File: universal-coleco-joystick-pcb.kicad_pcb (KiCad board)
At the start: 2 copper layers, 108 x 62.3 mm, 49 parts, among them J1 Sanwa Joystick, J2 DE9_Receptacle, J3 Conn_01x09_Socket, SW1 Arm, SW10 2, SW11 #, SW12 9, SW13 6, SW14 3, SW2 Fire, SW3 *, SW4 7, SW5 1, SW6 4, SW7 0, SW8 8, SW9 5

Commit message: Credit
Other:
- board text added: "1"
- board text added: "2"
- board text added: "3"
- board text added: "4"
- board text added: "5"
- board text added: "6"
- board text added: "7"
- board text added: "8"
- board text added: "9"
- board text added: "CV DIY Joystick (Sanwa Edition) v1 leadedsolder.com 2024"
- board text added: "Female DE9 (optional)"
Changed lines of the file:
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@@
 		(tags "Diode DO-41_SOD81 series Axial Horizontal pin pitch 10.16mm  length 5.2mm diameter 2.7mm")
 		(property "Reference" "D24"
-			(at 5.08 0 360)
+			(at 5.08 0 0)
 			(layer "F.SilkS")
 			(effects
@@
 		)
 		(property "Value" "D_45deg"
-			(at 5.08 2.47 360)
+			(at 5.08 2.47 0)
 			(layer "F.Fab")
 			(effects
@@
 		)
 		(fp_text user "${REFERENCE}"
-			(at 5.47 0 360)
+			(at 5.47 0 0)
 			(layer "F.Fab")
 			(effects
@@
 		)
 		(fp_text user "K"
-			(at 0 -2.1 360)
+			(at 0 -2.1 0)
 			(layer "F.Fab")
 			(effects
@@
 		(tags "9-pin D-Sub connector horizontal angled 90deg THT female pitch 2.77x2.84mm pin-PCB-offset 7.699999999999999mm mounting-holes-distance 25mm mounting-hole-offset 25mm")
 		(property "Reference" "J2"
-			(at -5.54 -2.8 360)
+			(at -5.54 -2.8 0)
 			(layer "F.SilkS")
 			(effects
@@
 		)
 		(property "Value" "DE9_Receptacle"
-			(at -5.54 18.61 360)
+			(at -5.54 18.61 0)
 			(layer "F.Fab")
 			(effects
@@
 		)
 		(fp_text user "${REFERENCE}"
-			(at -5.54 14.025 360)
+			(at -5.54 14.025 0)
 			(layer "F.Fab")
 			(effects
@@
 		)
 		(fp_text user "${REFERENCE}"
-			(at 0 10.16 360)
+			(at 0 10.16 0)
 			(layer "F.Fab")
 			(effects
@@
 		(layer "Edge.Cuts")
 	)
+	(gr_text "3"
+		(at 136.525 74.93 0)
+		(layer "B.SilkS")
+		(effects
+			(font
+				(size 1 1)
+				(thickness 0.1)
+			)
+			(justify left bottom mirror)
+		)
+	)
+	(gr_text "4"
+		(at 139.065 74.93 0)
+		(layer "B.SilkS")
+		(effects
+			(font
+				(size 1 1)
+				(thickness 0.1)
+			)
+			(justify left bottom mirror)
+		)
+	)
+	(gr_text "8"
+		(at 137.795 68.58 0)
+		(layer "B.SilkS")
+		(effects
+			(font
+				(size 1 1)
+				(thickness 0.1)
+			)
+			(justify left bottom mirror)
+		)
+	)
+	(gr_text "9"
+		(at 140.335 68.58 0)
+		(layer "B.SilkS")
+		(effects
+			(font
+				(size 1 1)
+				(thickness 0.1)
+			)
+			(justify left bottom mirror)
+		)
+	)
+	(gr_text "2"
+		(at 133.35 74.93 0)
+		(layer "B.SilkS")
+		(effects
+			(font
+				(size 1 1)
+				(thickness 0.1)
+			)
+			(justify left bottom mirror)
+		)
+	)
+	(gr_text "1"
+		(at 130.81 74.93 0)
+		(layer "B.SilkS")
+		(effects
+			(font
+				(size 1 1)
+				(thickness 0.1)
+			)
+			(justify left bottom mirror)
+		)
+	)
+	(gr_text "7"
+		(at 134.62 68.58 0)
+		(layer "B.SilkS")
+		(effects
+			(font
+				(size 1 1)
+				(thickness 0.1)
+			)
+			(justify left bottom mirror)
+		)
+	)
+	(gr_text "5"
+		(at 142.875 74.93 0)
+		(layer "B.SilkS")
+		(effects
+			(font
+				(size 1 1)
+				(thickness 0.1)
+			)
+			(justify left bottom mirror)
+		)
+	)
+	(gr_text "6"
+		(at 132.08 68.58 0)
+		(layer "B.SilkS")
+		(effects
+			(font
+				(size 1 1)
+				(thickness 0.1)
+			)
+			(justify left bottom mirror)
+		)
+	)
+	(gr_text "CV DIY Joystick (Sanwa Edition) v1 leadedsolder.com 2024"
+		(at 90.805 121.285 0)
+		(layer "F.SilkS")
+		(effects
+			(font
+				(size 1 1)
+				(thickness 0.1)
+			)
+			(justify left bottom)
+		)
+	)
 	(gr_text "Down"
 		(at 88.9 72.39 0)
@@
 		(layer "F.SilkS")
 		(effects
+			(font
+				(size 1 1)
+				(thickness 0.1)
+			)
+			(justify left bottom)
+		)
+	)
+	(gr_text "Female DE9 (optional)"
+		(at 127.635 66.04 0)
+		(layer "F.SilkS")
+		(effects

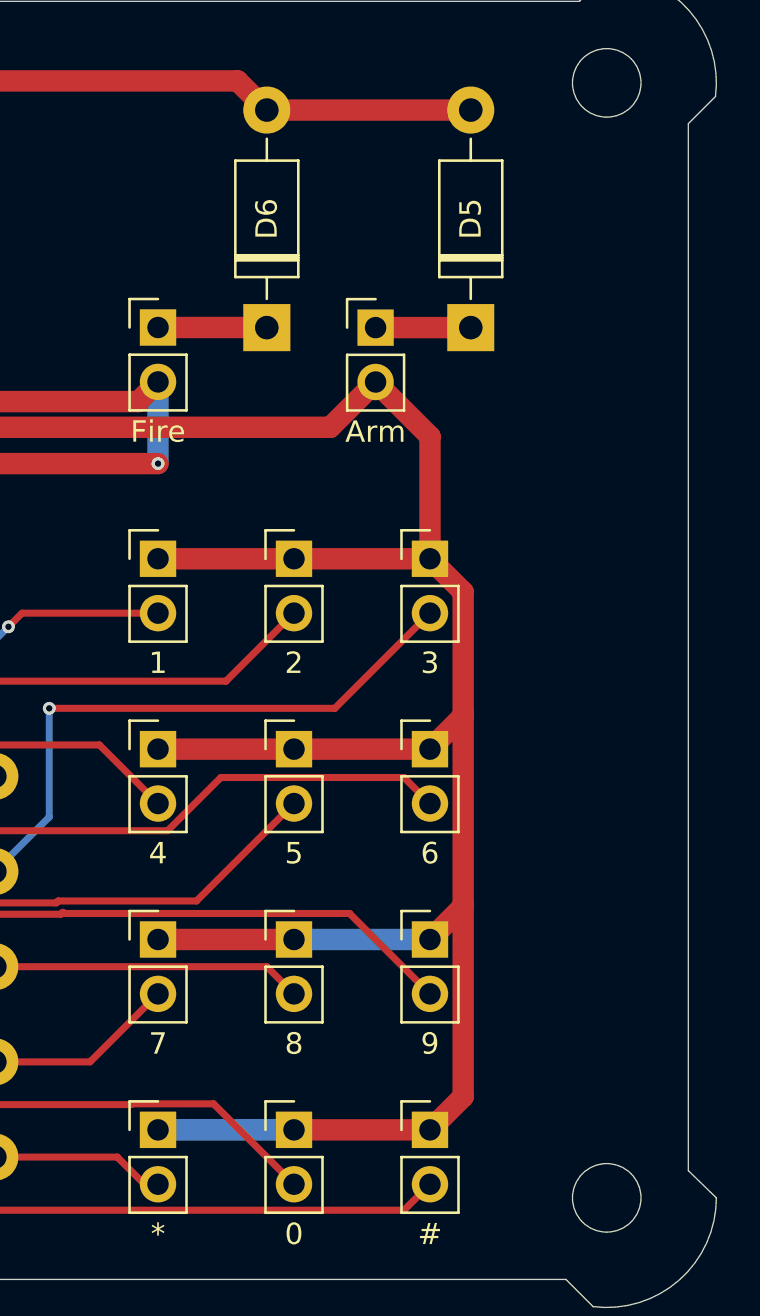
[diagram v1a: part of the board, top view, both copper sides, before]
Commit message: Linear KP header
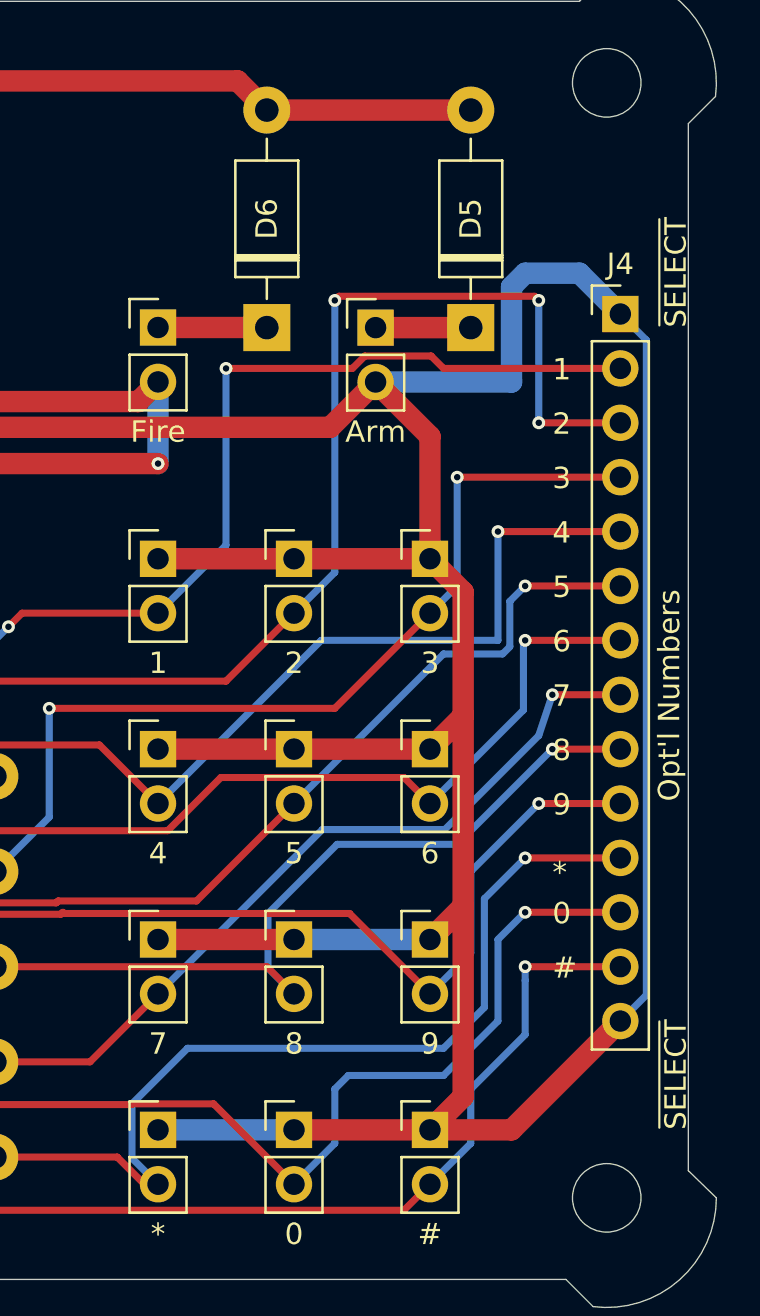
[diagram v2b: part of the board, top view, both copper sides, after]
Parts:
- added J4: Opt'l Numbers, Connector_PinHeader_2.54mm:PinHeader_1x14_P2.54mm_Vertical, F.Cu at (185.4, 76.8)
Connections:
- net Net-(D10-A) renamed /KP_7
- net Net-(D11-A) renamed /KP_1
- net Net-(D17-A) renamed /KP_8
- net Net-(D27-A) renamed /KP_3
- net Net-(D7-A) renamed /KP_STAR
- D12 pad 2: unconnected-(D12-A-Pad2) -> /KP_4
- D13 pad 2: unconnected-(D12-A-Pad2) -> /KP_4
- D14 pad 2: unconnected-(D12-A-Pad2) -> /KP_4
- D15 pad 2: unconnected-(D15-A-Pad2) -> /KP_0
- D16 pad 2: unconnected-(D15-A-Pad2) -> /KP_0
- D20 pad 2: unconnected-(D20-A-Pad2) -> /KP_5
- D21 pad 2: unconnected-(D20-A-Pad2) -> /KP_5
- D22 pad 2: unconnected-(D22-A-Pad2) -> /KP_2
- D23 pad 2: unconnected-(D23-A-Pad2) -> /KP_OCTOTHORPE
- D24 pad 2: unconnected-(D23-A-Pad2) -> /KP_OCTOTHORPE
- D25 pad 2: unconnected-(D25-A-Pad2) -> /KP_9
- D26 pad 2: unconnected-(D26-A-Pad2) -> /KP_6
- SW10 pad 2: unconnected-(D22-A-Pad2) -> /KP_2
- SW11 pad 2: unconnected-(D23-A-Pad2) -> /KP_OCTOTHORPE
- SW12 pad 2: unconnected-(D25-A-Pad2) -> /KP_9
- SW13 pad 2: unconnected-(D26-A-Pad2) -> /KP_6
- SW6 pad 2: unconnected-(D12-A-Pad2) -> /KP_4
- SW7 pad 2: unconnected-(D15-A-Pad2) -> /KP_0
- SW9 pad 2: unconnected-(D20-A-Pad2) -> /KP_5
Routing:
- net /KP_4: track 0.00 -> 82.2 mm, vias 0 -> 1
- net /KP_0: track 0.00 -> 81.8 mm, vias 0 -> 1
- net /KP_OCTOTHORPE: track 0.00 -> 79.5 mm, vias 0 -> 1
- net /KP_6: track 0.00 -> 76.8 mm, vias 0 -> 1
- net /KP_5: track 0.00 -> 69.7 mm, vias 0 -> 2
- net /KP_9: track 0.00 -> 65.0 mm, vias 0 -> 1
- net /KP_2: track 0.00 -> 63.2 mm, vias 0 -> 3
- net unconnected-(D23-A-Pad2): track 63.1 -> 0.00 mm
- net unconnected-(D26-A-Pad2): track 62.9 -> 0.00 mm
- net /~{Select}: track 141.6 -> 203.6 mm
- net unconnected-(D15-A-Pad2): track 57.6 -> 0.00 mm
- net unconnected-(D12-A-Pad2): track 52.4 -> 0.00 mm
- net unconnected-(D25-A-Pad2): track 50.2 -> 0.00 mm
- net unconnected-(D20-A-Pad2): track 49.0 -> 0.00 mm, vias 1 -> 0
- net /KP_STAR: track 36.0 -> 70.8 mm, vias 0 -> 1
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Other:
- board text added: "#"
- board text added: "*"
- board text added: "0"
- board text added: "~{SELECT}"

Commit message: Release v1 to JLC
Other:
- board text added: "2024-v1"
- board text added: "CV DIY Control leadedsolder.com"
- board text removed: "CV DIY Joystick (Sanwa Edition) v1 leadedsolder.com 2024"
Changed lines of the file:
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@@
 			(outputformat 1)
 			(mirror no)
-			(drillshape 1)
+			(drillshape 0)
 			(scaleselection 1)
-			(outputdirectory "")
+			(outputdirectory "cv-diy-joystick-proto1")
 		)
 	)
@@
 		)
 	)
+	(gr_rect
+		(start 94.615 91.44)
+		(end 100.33 120.015)
+		(stroke
+			(width 0.1)
+			(type solid)
+		)
+		(fill solid)
+		(layer "F.SilkS")
+	)
 	(gr_arc
 		(start 86.995 123.229533)
@@
 		)
 	)
-	(gr_text "CV DIY Joystick (Sanwa Edition) v1 leadedsolder.com 2024"
-		(at 90.805 121.285 0)
+	(gr_text "CV DIY Control\nleadedsolder.com"
+		(at 94 80.6 90)
 		(layer "F.SilkS")
 		(effects
 			(font
-				(size 1 1)
-				(thickness 0.1)
+				(size 3 3)
+				(thickness 0.5)
+				(bold yes)
+				(italic yes)
 			)
-			(justify left bottom)
+			(justify right bottom)
 		)
 	)
@@
 		(effects
 			(font
+				(size 1 1)
+				(thickness 0.1)
+			)
+			(justify left bottom)
+		)
+	)
+	(gr_text "2024-v1"
+		(at 96.52 90.805 90)
+		(layer "F.SilkS")
+		(effects
+			(font

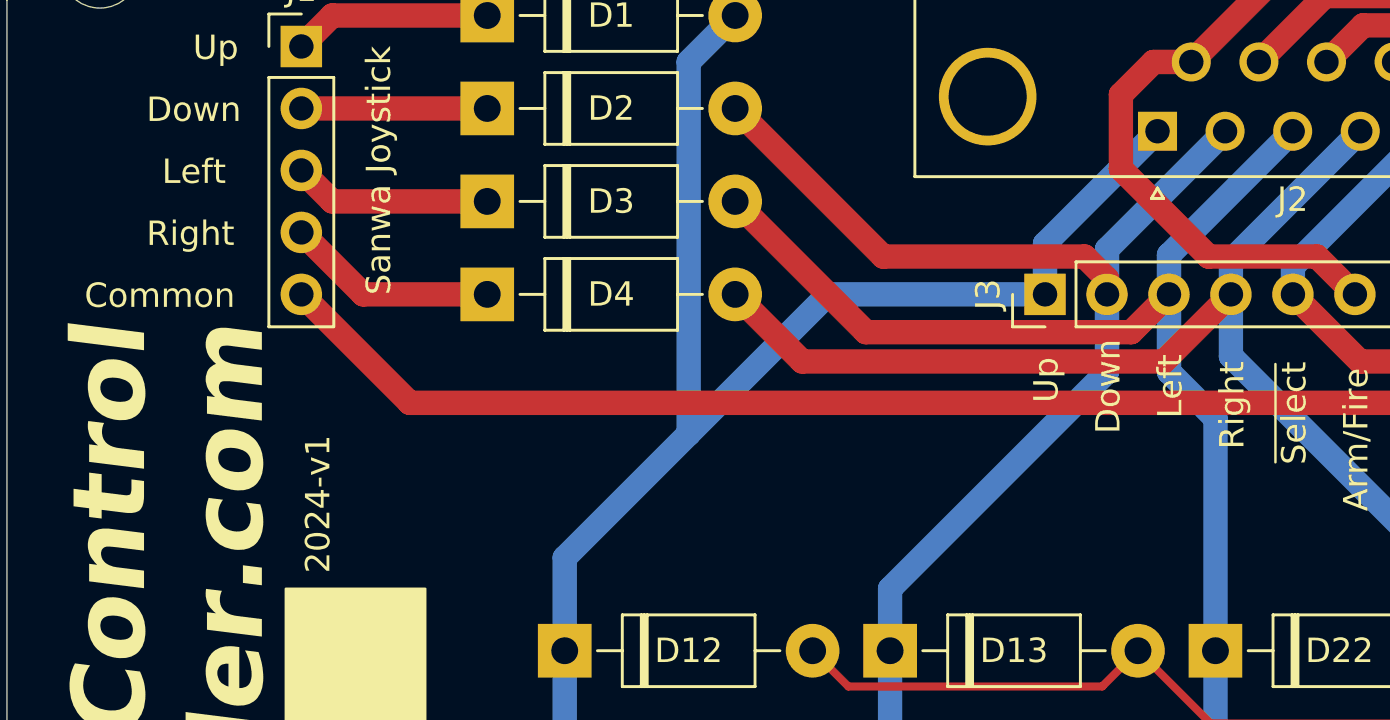
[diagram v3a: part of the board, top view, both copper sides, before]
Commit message: UDRL not UDLR joystick error
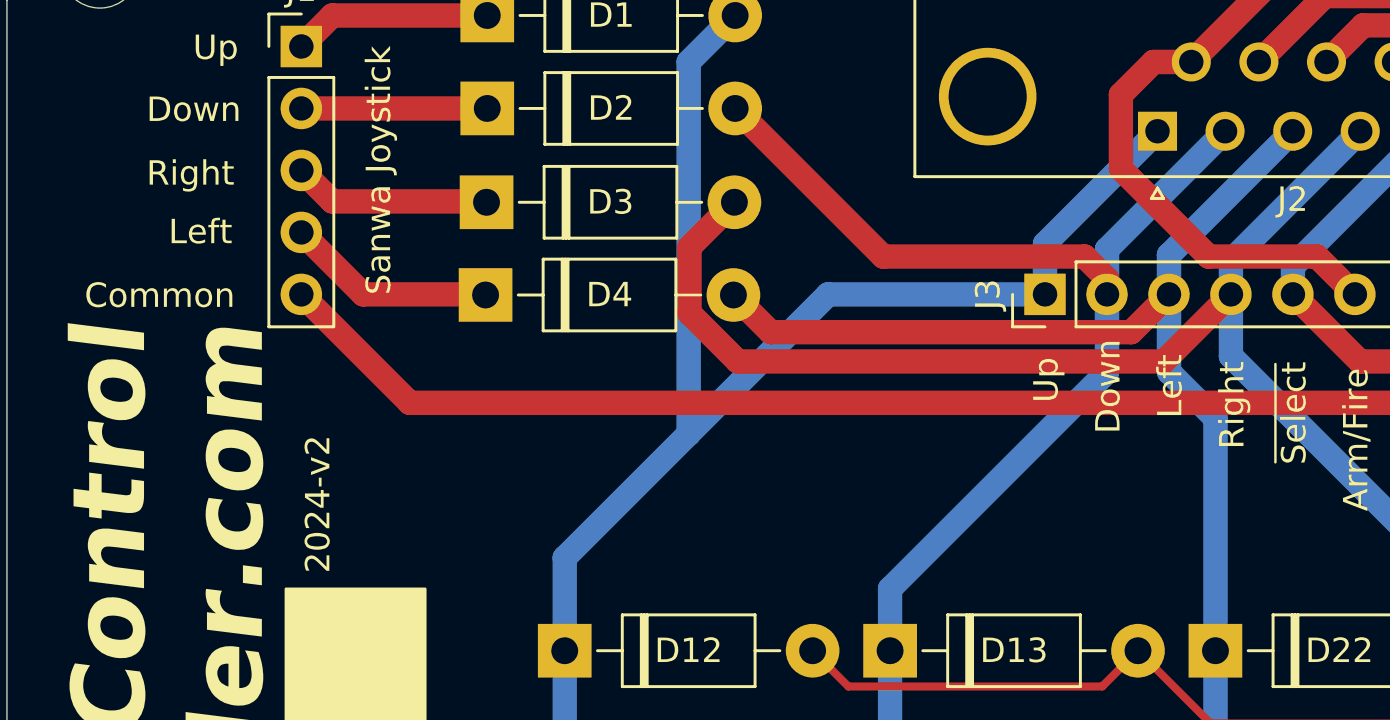
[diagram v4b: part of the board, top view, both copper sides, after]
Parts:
- moved D4 0.07 mm to (102.8, 79.4)
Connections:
- D3 pad 2: /Left -> /Right
- D4 pad 2: /Right -> /Left
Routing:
- net /Right: track 73.6 -> 80.4 mm
- net /Left: track 67.0 -> 65.5 mm
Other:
- board text added: "2024-v2"
- board text removed: "2024-v1"
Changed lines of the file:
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@@
 	(footprint "Diode_THT:D_DO-41_SOD81_P10.16mm_Horizontal"
 		(layer "F.Cu")
-		(at 102.87 79.375)
+		(at 102.8 79.4)
 		(descr "Diode, DO-41_SOD81 series, Axial, Horizontal, pin pitch=10.16mm, , length*diameter=5.2*2.7mm^2, , http://www.diodes.com/_files/packages/DO-41%20(Plastic).pdf")
 		(tags "Diode DO-41_SOD81 series Axial Horizontal pin pitch 10.16mm  length 5.2mm diameter 2.7mm")
@@
 			(layers "*.Cu" "*.Mask")
 			(remove_unused_layers no)
-			(net 8 "/Right")
+			(net 5 "/Left")
 			(pinfunction "A")
 			(pintype "passive")
@@
 	(footprint "Diode_THT:D_DO-41_SOD81_P10.16mm_Horizontal"
 		(layer "F.Cu")
-		(at 102.87 75.565)
+		(at 102.84 75.6)
 		(descr "Diode, DO-41_SOD81 series, Axial, Horizontal, pin pitch=10.16mm, , length*diameter=5.2*2.7mm^2, , http://www.diodes.com/_files/packages/DO-41%20(Plastic).pdf")
 		(tags "Diode DO-41_SOD81 series Axial Horizontal pin pitch 10.16mm  length 5.2mm diameter 2.7mm")
@@
 			(layers "*.Cu" "*.Mask")
 			(remove_unused_layers no)
-			(net 5 "/Left")
+			(net 8 "/Right")
 			(pinfunction "A")
 			(pintype "passive")
@@
 	(gr_text "Common"
 		(at 86.36 80.01 0)
-		(layer "F.SilkS")
+		(layer "F.SilkS" knockout)
 		(effects
 			(font
@@
 	)
 	(gr_text "Right"
-		(at 88.9 77.47 0)
+		(at 88.9 75 0)
 		(layer "F.SilkS")
 		(effects
@@
 	)
 	(gr_text "Left"
-		(at 89.535 74.93 0)
+		(at 89.8 77.4 0)
 		(layer "F.SilkS")
 		(effects
@@
 		)
 	)
-	(gr_text "2024-v1"
+	(gr_text "2024-v2"
 		(at 96.52 90.805 90)
 		(layer "F.SilkS")
@@
 	(segment
 		(start 129.26 80.925)
-		(end 118.39 80.925)
+		(end 114.485 80.925)
 		(width 1)
 		(layer "F.Cu")
@@
 	)
 	(segment
-		(start 130.81 79.375)
-		(end 129.26 80.925)
+		(start 114.485 80.925)
+		(end 112.96 79.4)
 		(width 1)
 		(layer "F.Cu")
@@
 	)
 	(segment
-		(start 118.39 80.925)
-		(end 113.03 75.565)
+		(start 130.81 79.375)
+		(end 129.26 80.925)
 		(width 1)
 		(layer "F.Cu")
@@
 	)
 	(segment
-		(start 115.78 82.125)
+		(start 111.16 80.145585)
+		(end 111.16 77.44)
+		(width 1)
+		(layer "F.Cu")
+		(net 8)
+	)
+	(segment
+		(start 130.6 82.125)
+		(end 113.139415 82.125)
+		(width 1)
+		(layer "F.Cu")
+		(net 8)
+	)
+	(segment
+		(start 133.35 79.375)
 		(end 130.6 82.125)
 		(width 1)
@@
 	)
 	(segment
-		(start 113.03 79.375)
-		(end 115.78 82.125)
+		(start 111.16 77.44)
+		(end 113 75.6)
 		(width 1)
 		(layer "F.Cu")
@@
 	)
 	(segment
-		(start 130.6 82.125)
-		(end 133.35 79.375)
+		(start 113.139415 82.125)
+		(end 111.16 80.145585)
 		(width 1)
 		(layer "F.Cu")
